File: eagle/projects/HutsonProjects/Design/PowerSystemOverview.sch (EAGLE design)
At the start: 27 parts, among them U1 MCP7384XX, U3 MT3608, U4 LTC3531ES6-3_3

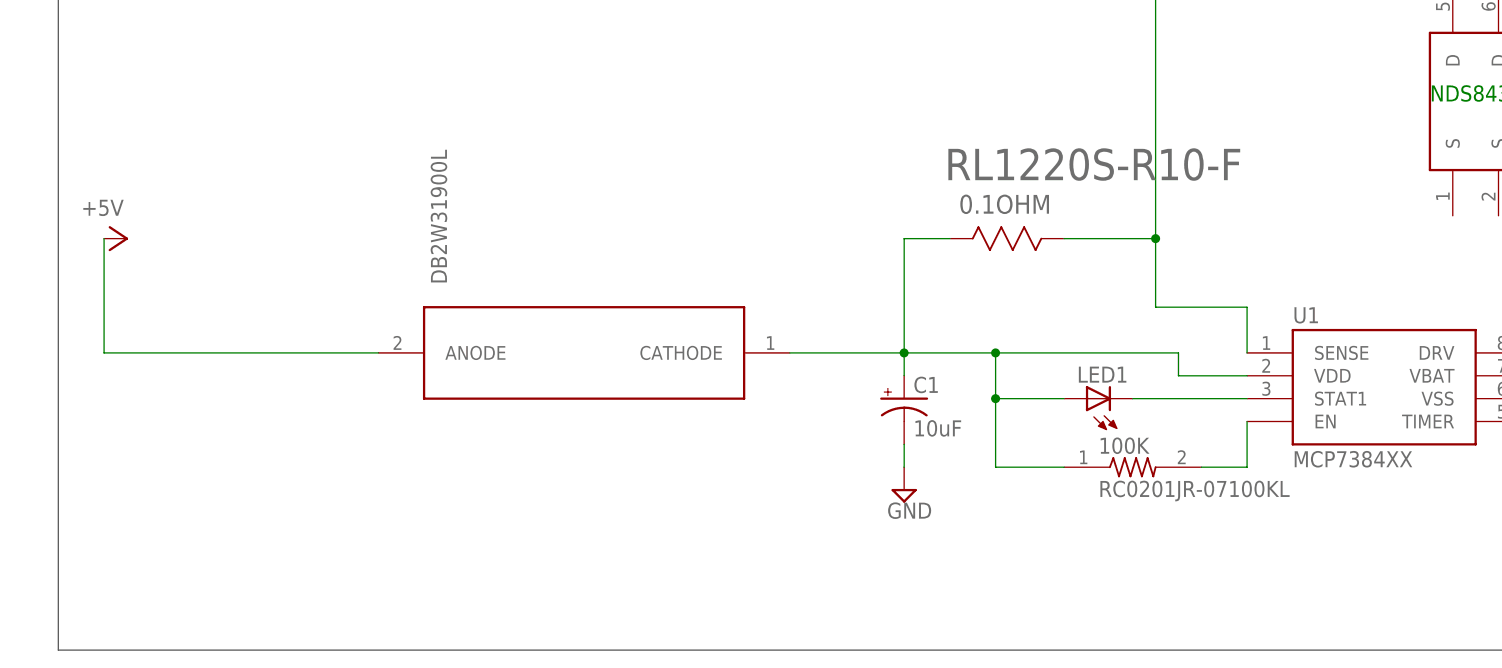
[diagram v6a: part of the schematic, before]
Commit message: USB Mini Power In and New Resistor
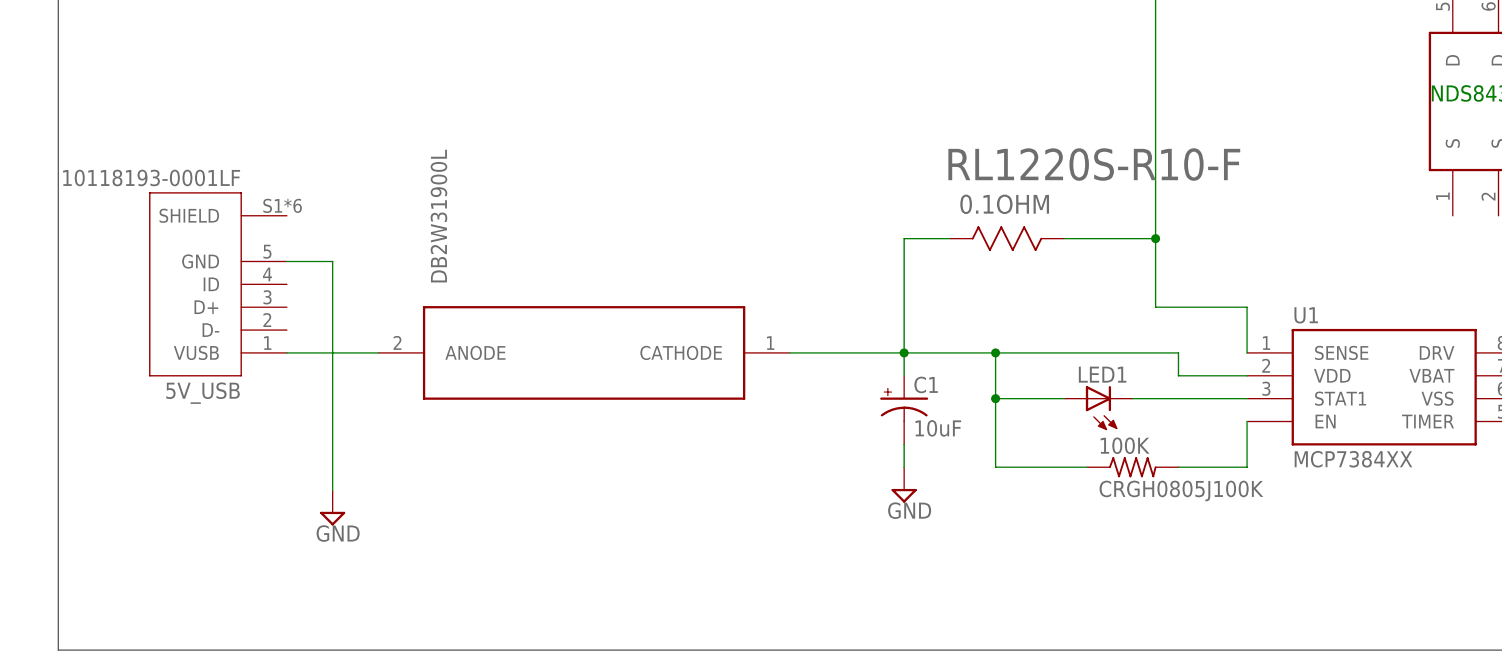
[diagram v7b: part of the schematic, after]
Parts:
- added 5V_USB: 10118193-0001LF, 10118193-0001LF:10118193-0001LF
- 100K: value RC0201JR-07100KL -> CRGH0805J100K; device RC0201JR-07100KL:RC0201JR-07100KL -> CRGH0805J100K:CRGH0805J100K
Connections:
- removed net CONT_ON_SOLENOID: U$5.ANODE
- new net N$12: 5V_USB.VUSB, U$5.ANODE
- net GND: now also 5V_USB.GND
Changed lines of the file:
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@@
 <parts>
 <part name="U1" library="SparkFun-IC-Power" deviceset="MCP7384XX" device=""/>
-<part name="P+1" library="supply1" library_urn="urn:adsk.eagle:library:371" deviceset="+5V" device=""/>
 <part name="C1" library="SparkFun-Capacitors" deviceset="10UF-POLAR" device="-0603-6.3V-20%(TANT)" value="10uF"/>
 <part name="SUPPLY1" library="supply2" library_urn="urn:adsk.eagle:library:372" deviceset="GND" device=""/>
@@
 <part name="U$6" library="DB2W31900L" deviceset="DB2W31900" device=""/>
 <part name="0.1OHM" library="RL1220S-R10-F" deviceset="RL1220S-R10-F" device=""/>
-<part name="100K" library="RC0201JR-07100KL" deviceset="RC0201JR-07100KL" device=""/>
 <part name="330" library="3521330RFT" deviceset="3521330RFT" device=""/>
 <part name="2.7K" library="ERA-3AEB272V" deviceset="ERA-3AEB272V" device=""/>
+<part name="5V_USB" library="10118193-0001LF" deviceset="10118193-0001LF" device=""/>
+<part name="SUPPLY6" library="supply2" library_urn="urn:adsk.eagle:library:372" deviceset="GND" device=""/>
+<part name="100K" library="CRGH0805J100K" deviceset="CRGH0805J100K" device=""/>
 </parts>
 <sheets>
@@
 <attribute name="NAME" x="30.48" y="97.282" size="1.778" layer="95"/>
 </instance>
-<instance part="P+1" gate="1" x="-99.06" y="106.68" smashed="yes" rot="R270">
-<attribute name="VALUE" x="-104.14" y="109.22" size="1.778" layer="96"/>
-</instance>
 <instance part="C1" gate="G$1" x="-12.7" y="88.9" smashed="yes">
 <attribute name="NAME" x="-11.684" y="89.535" size="1.778" layer="95" font="vector"/>
@@
 <attribute name="NAME" x="-6.628359375" y="109.451509375" size="2.084990625" layer="95" ratio="10" rot="SR0"/>
 </instance>
+<instance part="330" gate="G$1" x="104.14" y="111.76" smashed="yes">
+<attribute name="NAME" x="100.33" y="113.2586" size="1.778" layer="95"/>
+<attribute name="VALUE" x="100.33" y="108.458" size="1.778" layer="96"/>
+</instance>
+<instance part="2.7K" gate="G$1" x="154.94" y="96.52" smashed="yes" rot="R90">
+<attribute name="NAME" x="153.44091875" y="92.708790625" size="1.77856875" layer="95" rot="R90"/>
+<attribute name="VALUE" x="158.242209375" y="92.709759375" size="1.778109375" layer="96" rot="R90"/>
+</instance>
+<instance part="5V_USB" gate="G$1" x="-91.44" y="101.6" smashed="yes" rot="R180">
+<attribute name="NAME" x="-86.35835" y="90.6714" size="1.778" layer="95" rot="R180"/>
+<attribute name="VALUE" x="-86.35806875" y="114.3097" size="1.778" layer="96" rot="R180"/>
+</instance>
+<instance part="SUPPLY6" gate="GND" x="-76.2" y="76.2" smashed="yes">
+<attribute name="VALUE" x="-78.105" y="73.025" size="1.778" layer="96"/>
+</instance>
 <instance part="100K" gate="G$1" x="12.7" y="81.28" smashed="yes">
 <attribute name="NAME" x="8.89" y="82.7786" size="1.778" layer="95"/>
 <attribute name="VALUE" x="8.89" y="77.978" size="1.778" layer="96"/>
-</instance>
-<instance part="330" gate="G$1" x="104.14" y="111.76" smashed="yes">
-<attribute name="NAME" x="100.33" y="113.2586" size="1.778" layer="95"/>
-<attribute name="VALUE" x="100.33" y="108.458" size="1.778" layer="96"/>
-</instance>
-<instance part="2.7K" gate="G$1" x="154.94" y="96.52" smashed="yes" rot="R90">
-<attribute name="NAME" x="153.44091875" y="92.708790625" size="1.77856875" layer="95" rot="R90"/>
-<attribute name="VALUE" x="158.242209375" y="92.709759375" size="1.778109375" layer="96" rot="R90"/>
 </instance>
 </instances>
@@
 <wire x1="-2.54" y1="93.98" x2="-12.7" y2="93.98" width="0.1524" layer="91"/>
 <junction x="-2.54" y="93.98"/>
+<wire x1="-2.54" y1="81.28" x2="7.62" y2="81.28" width="0.1524" layer="91"/>
 <pinref part="100K" gate="G$1" pin="1"/>
-<wire x1="-2.54" y1="81.28" x2="5.08" y2="81.28" width="0.1524" layer="91"/>
 </segment>
 </net>
@@
 <wire x1="154.94" y1="91.44" x2="154.94" y2="81.28" width="0.1524" layer="91"/>
 </segment>
-</net>
-<net name="CONT_ON_SOLENOID" class="0">
-<segment>
-<pinref part="P+1" gate="1" pin="+5V"/>
-<wire x1="-101.6" y1="106.68" x2="-101.6" y2="93.98" width="0.1524" layer="91"/>
-<pinref part="U$5" gate="G$1" pin="ANODE"/>
-<wire x1="-101.6" y1="93.98" x2="-71.12" y2="93.98" width="0.1524" layer="91"/>
+<segment>
+<pinref part="5V_USB" gate="G$1" pin="GND"/>
+<wire x1="-81.28" y1="104.14" x2="-76.2" y2="104.14" width="0.1524" layer="91"/>
+<wire x1="-76.2" y1="104.14" x2="-76.2" y2="78.74" width="0.1524" layer="91"/>
+<pinref part="SUPPLY6" gate="GND" pin="GND"/>
 </segment>
 </net>
@@
 <pinref part="U1" gate="G$1" pin="EN"/>
 <wire x1="25.4" y1="81.28" x2="25.4" y2="86.36" width="0.1524" layer="91"/>
+<wire x1="17.78" y1="81.28" x2="25.4" y2="81.28" width="0.1524" layer="91"/>
 <pinref part="100K" gate="G$1" pin="2"/>
-<wire x1="20.32" y1="81.28" x2="25.4" y2="81.28" width="0.1524" layer="91"/>
 </segment>
 </net>
@@
 </segment>
 </net>
+<net name="N$12" class="0">
+<segment>
+<pinref part="5V_USB" gate="G$1" pin="VUSB"/>
+<pinref part="U$5" gate="G$1" pin="ANODE"/>
+<wire x1="-81.28" y1="93.98" x2="-71.12" y2="93.98" width="0.1524" layer="91"/>
+</segment>
+</net>

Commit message: 330 ohm resistor chip
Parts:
- removed 330: 3521330RFT, 3521330RFT:3521330RFT
- added R1: ERJP6WF3300V, ERJP6WF3300V:ERJP6WF3300V
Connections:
- net N$16: now also R1.1; no longer 330.1
- net N$7: now also R1.2; no longer 330.2
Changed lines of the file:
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@@
 <part name="U$6" library="DB2W31900L" deviceset="DB2W31900" device=""/>
 <part name="0.1OHM" library="RL1220S-R10-F" deviceset="RL1220S-R10-F" device=""/>
-<part name="330" library="3521330RFT" deviceset="3521330RFT" device=""/>
 <part name="2.7K" library="ERA-3AEB272V" deviceset="ERA-3AEB272V" device=""/>
 <part name="5V_USB" library="10118193-0001LF" deviceset="10118193-0001LF" device=""/>
 <part name="SUPPLY6" library="supply2" library_urn="urn:adsk.eagle:library:372" deviceset="GND" device=""/>
 <part name="100K" library="CRGH0805J100K" deviceset="CRGH0805J100K" device=""/>
+<part name="R1" library="ERJP6WF3300V" deviceset="ERJP6WF3300V" device=""/>
 </parts>
 <sheets>
@@
 <attribute name="NAME" x="-6.628359375" y="109.451509375" size="2.084990625" layer="95" ratio="10" rot="SR0"/>
 </instance>
-<instance part="330" gate="G$1" x="104.14" y="111.76" smashed="yes">
-<attribute name="NAME" x="100.33" y="113.2586" size="1.778" layer="95"/>
-<attribute name="VALUE" x="100.33" y="108.458" size="1.778" layer="96"/>
-</instance>
 <instance part="2.7K" gate="G$1" x="154.94" y="96.52" smashed="yes" rot="R90">
 <attribute name="NAME" x="153.44091875" y="92.708790625" size="1.77856875" layer="95" rot="R90"/>
@@
 <attribute name="NAME" x="8.89" y="82.7786" size="1.778" layer="95"/>
 <attribute name="VALUE" x="8.89" y="77.978" size="1.778" layer="96"/>
+</instance>
+<instance part="R1" gate="G$1" x="101.6" y="111.76" smashed="yes">
+<attribute name="NAME" x="97.79" y="113.2586" size="1.778" layer="95"/>
+<attribute name="VALUE" x="97.79" y="108.458" size="1.778" layer="96"/>
 </instance>
 </instances>
@@
 <bus name="B$2">
 <segment>
-<wire x1="93.98" y1="139.7" x2="93.98" y2="60.96" width="0.508" layer="92"/>
 <wire x1="93.98" y1="60.96" x2="172.72" y2="60.96" width="0.508" layer="92"/>
 <wire x1="172.72" y1="60.96" x2="172.72" y2="121.92" width="0.508" layer="92"/>
@@
 <wire x1="111.76" y1="111.76" x2="119.38" y2="111.76" width="0.1524" layer="91"/>
 <wire x1="111.76" y1="104.14" x2="111.76" y2="111.76" width="0.1524" layer="91"/>
-<pinref part="330" gate="G$1" pin="2"/>
+<pinref part="R1" gate="G$1" pin="2"/>
 <wire x1="109.22" y1="111.76" x2="111.76" y2="111.76" width="0.1524" layer="91"/>
 <junction x="111.76" y="111.76"/>
@@
 <pinref part="LI-ION" gate="G$1" pin="+"/>
 <wire x1="88.9" y1="109.22" x2="88.9" y2="111.76" width="0.1524" layer="91"/>
-<wire x1="88.9" y1="111.76" x2="96.52" y2="111.76" width="0.1524" layer="91"/>
-<wire x1="96.52" y1="111.76" x2="96.52" y2="121.92" width="0.1524" layer="91"/>
-<wire x1="96.52" y1="121.92" x2="149.86" y2="121.92" width="0.1524" layer="91"/>
+<wire x1="88.9" y1="111.76" x2="88.9" y2="121.92" width="0.1524" layer="91"/>
+<wire x1="88.9" y1="121.92" x2="149.86" y2="121.92" width="0.1524" layer="91"/>
 <pinref part="C5" gate="G$1" pin="1"/>
 <pinref part="L1" gate="G$1" pin="1"/>
@@
 <wire x1="83.82" y1="213.36" x2="111.76" y2="213.36" width="0.1524" layer="91"/>
 <junction x="111.76" y="213.36"/>
-<pinref part="330" gate="G$1" pin="1"/>
-<wire x1="96.52" y1="111.76" x2="99.06" y2="111.76" width="0.1524" layer="91"/>
-<junction x="96.52" y="111.76"/>
-</segment>
-</net>
+<pinref part="R1" gate="G$1" pin="1"/>
+<wire x1="88.9" y1="111.76" x2="93.98" y2="111.76" width="0.1524" layer="91"/>
+<junction x="88.9" y="111.76"/>
+</segment>
+</net>
